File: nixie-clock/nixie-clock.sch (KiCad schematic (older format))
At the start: 69 parts, among them J1 Barrel_Jack, J2 Conn_01x02, J3 Conn_01x02, Q1 2N7002, Q2 2N7002, Q3 2N7002, Q4 2N7002, Q5 2N7002, Q6 Q_Photo_NPN, Q7 PSMN014-80YL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

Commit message: Top layer ground plane and stitching
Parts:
- added J4, J5, J6, J7, J8: Conn_01x01_MountingPin, custom-parts:4MM_Mounting_Hole, symbol Connector_Generic_MountingPin:Conn_01x01_MountingPin
- U1: symbol RF_Module:ESP32-WROOM-32D -> custom-parts:ESP32-WROOM-32D
- U6: footprint Package_SO:SOIC-16W_7.5x10.3mm_P1.27mm -> Package_SO:SO-8_5.3x6.2mm_P1.27mm; symbol Timer_RTC:DS3231M -> Timer_RTC:DS3231MZ
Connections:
- net RTL_RST is gone; now on net RTC_RST: U6.4 (~RST)
- net +3V3: now also U6.6 (VBAT); no longer U6.2 (VCC)
- net GND: now also U1.39 (GND), U6.2 (VCC), J4.1 (Pin_1), J4.MP (MountPin), J5.1 (Pin_1), J5.MP (MountPin), J6.1 (Pin_1), J6.MP (MountPin), J7.1 (Pin_1), J7.MP (MountPin), J8.1 (Pin_1), J8.MP (MountPin); no longer U6.10 (GND), U6.11 (GND), U6.12 (GND), U6.13 (GND), U6.14 (VBAT), U6.6 (GND), U6.7 (GND), U6.8 (GND), U6.9 (GND)
- net RTC_INT: now also U1.9 (IO33); no longer U1.37 (IO23)
- net RTC_SCL: now also U6.8 (SCL); no longer U6.16 (SCL)
- net RTC_SDA: now also R8.2, U6.7 (SDA)
- net at U2.28 (CLK), U3.28 (CLK): now also Q2.3 (D), R2.2; no longer Q1.3 (D), R1.2
- removed net RTL_SDA: R8.2, U6.15 (SDA)
- new net: Q1.3 (D), R1.2, U2.32 (DATA_IN)
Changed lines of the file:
@@
 $EndDescr
 $Comp
-L RF_Module:ESP32-WROOM-32D U1
+L custom-parts:ESP32-WROOM-32D U1
 U 1 1 5C1B096D
 P 1750 2500
@@
 Wire Wire Line
 	4700 3400 7850 3400
-Wire Wire Line
-	7850 3400 7850 1550
-Wire Wire Line
-	7850 1550 8850 1550
 Connection ~ 4300 1750
 Wire Wire Line
 	4300 1750 4300 1800
 Wire Wire Line
-	7750 1450 7750 3300
-Wire Wire Line
 	7750 3300 3950 3300
 Wire Wire Line
@@
 	3950 1750 3500 1750
 Wire Wire Line
-	7750 1450 8700 1450
+	7850 1450 8700 1450
 Connection ~ 3500 1750
 Wire Wire Line
@@
 $EndComp
 $Comp
-L Timer_RTC:DS3231M U6
+L Timer_RTC:DS3231MZ U6
 U 1 1 5C31CD5B
 P 2500 8100
 F 0 "U6" H 2500 7614 50  0000 C CNN
 F 1 "DS3231M" H 2500 7523 50  0000 C CNN
-F 2 "Package_SO:SOIC-16W_7.5x10.3mm_P1.27mm" H 2500 7500 50  0001 C CNN
+F 2 "Package_SO:SO-8_5.3x6.2mm_P1.27mm" H 2500 7500 50  0001 C CNN
 F 3 "http://datasheets.maximintegrated.com/en/ds/DS3231.pdf" H 2770 8150 50  0001 C CNN
 	1    2500 8100
@@
 RTC_SCL
 Text Label 1200 8000 0    50   ~ 0
-RTL_SDA
+RTC_SDA
 Text Label 1200 8300 0    50   ~ 0
-RTL_RST
+RTC_RST
 Wire Wire Line
 	2850 5850 3100 5850
@@
 	2350 3000 2450 3000
 Wire Wire Line
-	2350 2900 2450 2900
-Text Label 2450 2900 0    50   ~ 0
+	2350 3400 2450 3400
+Text Label 2450 3400 0    50   ~ 0
 RTC_INT
 Text Label 2450 3000 0    50   ~ 0
@@
 Wire Wire Line
 	9450 1000 9450 1050
+Wire Wire Line
+	7750 3300 7750 1550
+Wire Wire Line
+	7750 1550 8850 1550
+Wire Wire Line
+	7850 3400 7850 1450
+$Comp
+L Connector_Generic_MountingPin:Conn_01x01_MountingPin J4
+U 1 1 5C4AB747
+P 11500 12650
+F 0 "J4" H 11587 12616 50  0000 L CNN
+F 1 "Conn_01x01_MountingPin" H 11587 12525 50  0000 L CNN
+F 2 "custom-parts:4MM_Mounting_Hole" H 11500 12650 50  0001 C CNN
+F 3 "~" H 11500 12650 50  0001 C CNN
+	1    11500 12650
+	1    0    0    -1
+$EndComp
+$Comp
+L Connector_Generic_MountingPin:Conn_01x01_MountingPin J5
+U 1 1 5C4AB84B
+P 12800 12650
+F 0 "J5" H 12887 12616 50  0000 L CNN
+F 1 "Conn_01x01_MountingPin" H 12887 12525 50  0000 L CNN
+F 2 "custom-parts:4MM_Mounting_Hole" H 12800 12650 50  0001 C CNN
+F 3 "~" H 12800 12650 50  0001 C CNN
+	1    12800 12650
+	1    0    0    -1
+$EndComp
+$Comp
+L Connector_Generic_MountingPin:Conn_01x01_MountingPin J6
+U 1 1 5C4AB90F
+P 14100 12650
+F 0 "J6" H 14187 12616 50  0000 L CNN
+F 1 "Conn_01x01_MountingPin" H 14187 12525 50  0000 L CNN
+F 2 "custom-parts:4MM_Mounting_Hole" H 14100 12650 50  0001 C CNN
+F 3 "~" H 14100 12650 50  0001 C CNN
+	1    14100 12650
+	1    0    0    -1
+$EndComp
+$Comp
+L Connector_Generic_MountingPin:Conn_01x01_MountingPin J7
+U 1 1 5C4AB9DB
+P 15400 12650
+F 0 "J7" H 15487 12616 50  0000 L CNN
+F 1 "Conn_01x01_MountingPin" H 15487 12525 50  0000 L CNN
+F 2 "custom-parts:4MM_Mounting_Hole" H 15400 12650 50  0001 C CNN
+F 3 "~" H 15400 12650 50  0001 C CNN
+	1    15400 12650
+	1    0    0    -1
+$EndComp
+$Comp
+L power:GND #PWR0144
+U 1 1 5C4AC4F4
+P 11500 12950
+F 0 "#PWR0144" H 11500 12700 50  0001 C CNN
+F 1 "GND" H 11505 12777 50  0000 C CNN
+F 2 "" H 11500 12950 50  0001 C CNN
+F 3 "" H 11500 12950 50  0001 C CNN
+	1    11500 12950
+	1    0    0    -1
+$EndComp
+$Comp
+L power:GND #PWR0145
+U 1 1 5C4AC598
+P 12800 12950
+F 0 "#PWR0145" H 12800 12700 50  0001 C CNN
+F 1 "GND" H 12805 12777 50  0000 C CNN
+F 2 "" H 12800 12950 50  0001 C CNN
+F 3 "" H 12800 12950 50  0001 C CNN
+	1    12800 12950
+	1    0    0    -1
+$EndComp
+$Comp
+L power:GND #PWR0146
+U 1 1 5C4AC635
+P 14100 12950
+F 0 "#PWR0146" H 14100 12700 50  0001 C CNN
+F 1 "GND" H 14105 12777 50  0000 C CNN
+F 2 "" H 14100 12950 50  0001 C CNN
+F 3 "" H 14100 12950 50  0001 C CNN
+	1    14100 12950
+	1    0    0    -1
+$EndComp
+$Comp
+L power:GND #PWR0147
+U 1 1 5C4AC6D2
+P 15400 12950
+F 0 "#PWR0147" H 15400 12700 50  0001 C CNN
+F 1 "GND" H 15405 12777 50  0000 C CNN
+F 2 "" H 15400 12950 50  0001 C CNN
+F 3 "" H 15400 12950 50  0001 C CNN
+	1    15400 12950
+	1    0    0    -1
+$EndComp
+Wire Wire Line
+	11300 12650 11300 12850
+Wire Wire Line
+	11300 12850 11500 12850
+Wire Wire Line
+	11500 12950 11500 12850
+Connection ~ 11500 12850
+Wire Wire Line
+	12600 12650 12600 12850
+Wire Wire Line
+	12600 12850 12800 12850
+Wire Wire Line
+	12800 12850 12800 12950
+Connection ~ 12800 12850
+Wire Wire Line
+	13900 12650 13900 12850
+Wire Wire Line
+	13900 12850 14100 12850
+Wire Wire Line
+	14100 12950 14100 12850
+Connection ~ 14100 12850
+Wire Wire Line
+	15200 12650 15200 12850
+Wire Wire Line
+	15200 12850 15400 12850
+Wire Wire Line
+	15400 12850 15400 12950
+Connection ~ 15400 12850
+$Comp
+L Connector_Generic_MountingPin:Conn_01x01_MountingPin J8
+U 1 1 5C4B3E54
+P 16700 12650
+F 0 "J8" H 16787 12616 50  0000 L CNN
+F 1 "Conn_01x01_MountingPin" H 16787 12525 50  0000 L CNN
+F 2 "custom-parts:4MM_Mounting_Hole" H 16700 12650 50  0001 C CNN
+F 3 "~" H 16700 12650 50  0001 C CNN
+	1    16700 12650
+	1    0    0    -1
+$EndComp
+$Comp
+L power:GND #PWR0148
+U 1 1 5C4B3E5A
+P 16700 12950
+F 0 "#PWR0148" H 16700 12700 50  0001 C CNN
+F 1 "GND" H 16705 12777 50  0000 C CNN
+F 2 "" H 16700 12950 50  0001 C CNN
+F 3 "" H 16700 12950 50  0001 C CNN
+	1    16700 12950
+	1    0    0    -1
+$EndComp
+Wire Wire Line
+	16500 12650 16500 12850
+Wire Wire Line
+	16500 12850 16700 12850
+Wire Wire Line
+	16700 12850 16700 12950
+Connection ~ 16700 12850
 $EndSCHEMATC

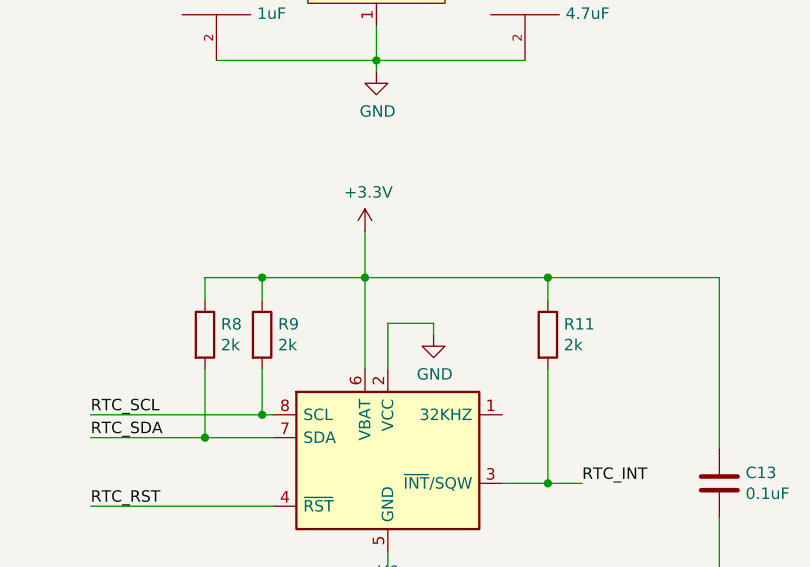
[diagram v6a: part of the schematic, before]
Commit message: Nixie Clock Fixes / Tweaks
- Connect TPS40210 power pad to ground.
- Exact board outlines
- Remove refs from mounting holes
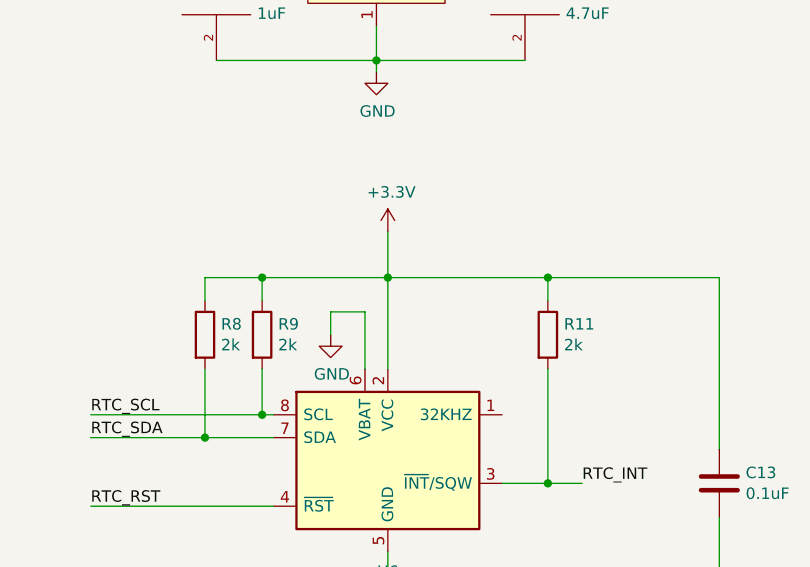
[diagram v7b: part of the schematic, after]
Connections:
- net +3V3: now also U6.2 (VCC); no longer U6.6 (VBAT)
- net GND: now also U6.6 (VBAT); no longer U6.2 (VCC)
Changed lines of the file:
@@
 L power:+3.3V #PWR0134
 U 1 1 5C729FDB
-P 2400 7100
-F 0 "#PWR0134" H 2400 6950 50  0001 C CNN
-F 1 "+3.3V" H 2415 7273 50  0000 C CNN
-F 2 "" H 2400 7100 50  0001 C CNN
-F 3 "" H 2400 7100 50  0001 C CNN
-	1    2400 7100
-	1    0    0    -1
-$EndComp
-Wire Wire Line
-	2400 7100 2400 7300
+P 2500 7100
+F 0 "#PWR0134" H 2500 6950 50  0001 C CNN
+F 1 "+3.3V" H 2515 7273 50  0000 C CNN
+F 2 "" H 2500 7100 50  0001 C CNN
+F 3 "" H 2500 7100 50  0001 C CNN
+	1    2500 7100
+	1    0    0    -1
+$EndComp
+Wire Wire Line
+	2500 7100 2500 7300
 $Comp
 L power:GND #PWR0135
@@
 Text Label 3350 8200 0    50   ~ 0
 RTC_INT
-$Comp
-L power:GND #PWR0136
-U 1 1 5C7BD655
-P 2700 7550
-F 0 "#PWR0136" H 2700 7300 50  0001 C CNN
-F 1 "GND" H 2705 7377 50  0000 C CNN
-F 2 "" H 2700 7550 50  0001 C CNN
-F 3 "" H 2700 7550 50  0001 C CNN
-	1    2700 7550
-	1    0    0    -1
-$EndComp
-Wire Wire Line
-	2700 7550 2700 7500
-Wire Wire Line
-	2700 7500 2500 7500
-Wire Wire Line
-	2500 7500 2500 7700
 Wire Wire Line
 	1200 7900 1950 7900
@@
 	1    0    0    -1
 $EndComp
-Connection ~ 2400 7300
-Wire Wire Line
-	2400 7300 2400 7700
+Connection ~ 2500 7300
 Wire Wire Line
 	1700 7400 1700 7300
@@
 Connection ~ 1950 7300
 Wire Wire Line
-	1950 7300 2400 7300
+	1950 7300 2500 7300
 Wire Wire Line
 	3200 7400 3200 7300
 Wire Wire Line
-	3200 7300 2400 7300
+	3200 7300 2500 7300
 Wire Wire Line
 	3200 7700 3200 8200
@@
 	16700 12850 16700 12950
 Connection ~ 16700 12850
+Wire Wire Line
+	2500 7300 2500 7700
+$Comp
+L power:GND #PWR0136
+U 1 1 5C5FD223
+P 2250 7550
+F 0 "#PWR0136" H 2250 7300 50  0001 C CNN
+F 1 "GND" H 2255 7377 50  0000 C CNN
+F 2 "" H 2250 7550 50  0001 C CNN
+F 3 "" H 2250 7550 50  0001 C CNN
+	1    2250 7550
+	1    0    0    -1
+$EndComp
+Wire Wire Line
+	2250 7550 2250 7450
+Wire Wire Line
+	2250 7450 2400 7450
+Wire Wire Line
+	2400 7450 2400 7700
 $EndSCHEMATC

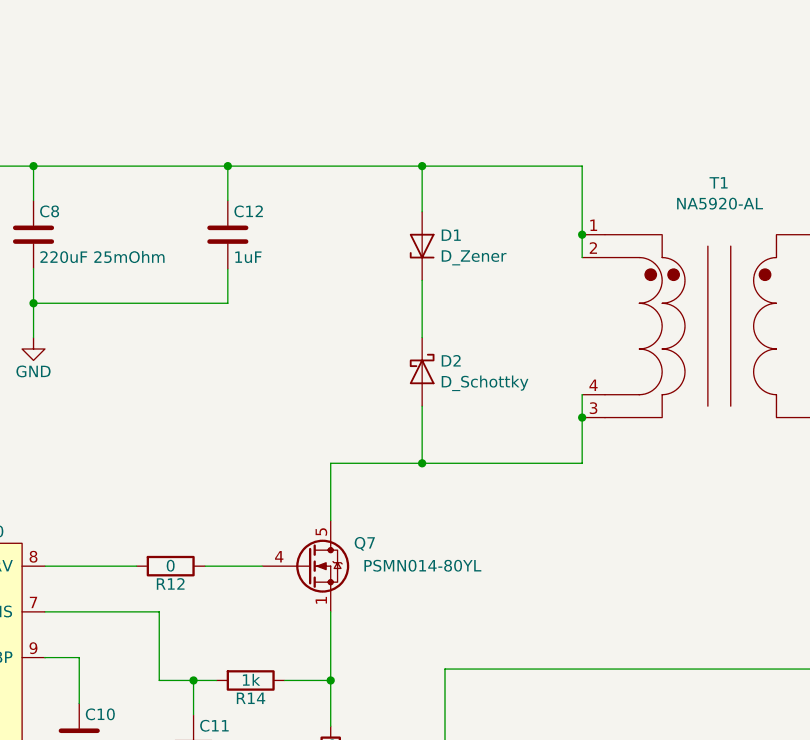
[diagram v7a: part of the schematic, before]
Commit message: HV power supply works, swap tubes to other side of board
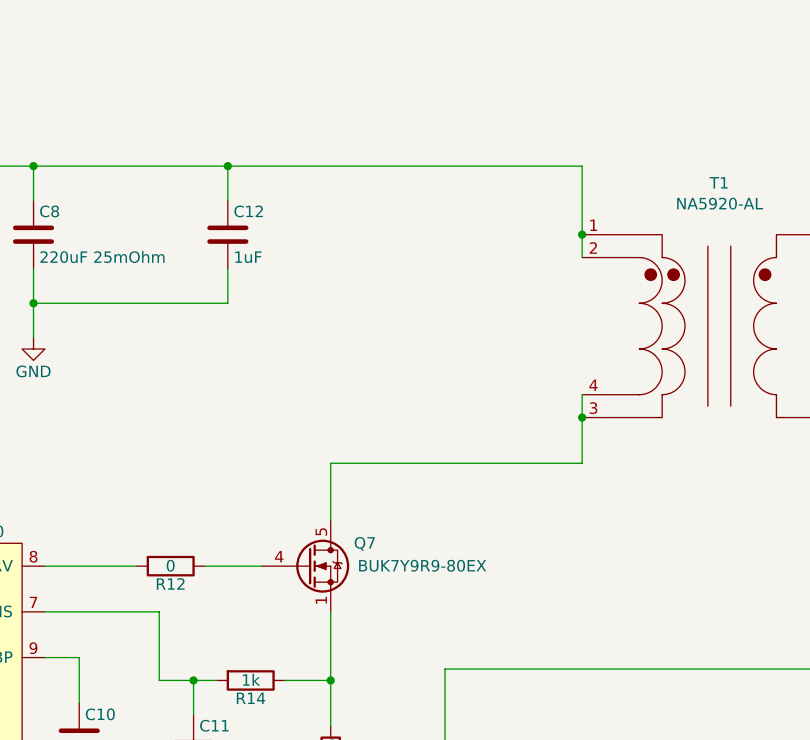
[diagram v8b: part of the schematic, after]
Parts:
- removed D1: D_Zener, Diode_SMD:D_SOD-123, symbol Device:D_Zener
- removed D2: D_Schottky, Diode_SMD:D_1206_3216Metric_Castellated, symbol Device:D_Schottky
- Q7: value PSMN014-80YL -> BUK7Y9R9-80EX
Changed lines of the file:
@@
 P 4100 13550
 F 0 "Q7" H 4350 13650 50  0000 C CNN
-F 1 "PSMN014-80YL" H 4600 13550 50  0000 C CNN
+F 1 "BUK7Y9R9-80EX" H 4600 13550 50  0000 C CNN
 F 2 "Package_TO_SOT_SMD:LFPAK56" H 4200 14000 50  0001 C CNN
 F 3 "https://assets.nexperia.com/documents/data-sheet/PSMN5R2-60YL.pdf" H 4100 13550 50  0001 C CNN
@@
 	1    0    0    -1
 $EndComp
-Wire Wire Line
-	5300 13100 4600 13100
 Wire Wire Line
 	4200 13100 4200 13350
@@
 Wire Wire Line
 	750  11650 750  11800
-Wire Wire Line
-	5300 11800 4600 11800
 Connection ~ 750  11800
 Wire Wire Line
@@
 	2550 4000 2550 4100
 $Comp
-L Device:D_Zener D1
-U 1 1 5C45A07C
-P 4600 12150
-F 0 "D1" V 4646 12071 50  0000 R CNN
-F 1 "D_Zener" V 4555 12071 50  0000 R CNN
-F 2 "Diode_SMD:D_SOD-123" H 4600 12150 50  0001 C CNN
-F 3 "~" H 4600 12150 50  0001 C CNN
-F 4 "BZT52-B75J" V 4600 12150 50  0001 C CNN "Part Number"
-	1    4600 12150
-	0    -1   -1   0
-$EndComp
-$Comp
-L Device:D_Schottky D2
-U 1 1 5C45A278
-P 4600 12700
-F 0 "D2" V 4554 12779 50  0000 L CNN
-F 1 "D_Schottky" V 4645 12779 50  0000 L CNN
-F 2 "Diode_SMD:D_1206_3216Metric_Castellated" H 4600 12700 50  0001 C CNN
-F 3 "~" H 4600 12700 50  0001 C CNN
-F 4 "CD1206-B2100" V 4600 12700 50  0001 C CNN "Part Number"
-	1    4600 12700
-	0    1    1    0
-$EndComp
-Wire Wire Line
-	4600 11800 4600 12000
-Connection ~ 4600 11800
-Wire Wire Line
-	4600 11800 3750 11800
-Wire Wire Line
-	4600 12300 4600 12550
-Wire Wire Line
-	4600 12850 4600 13100
-Connection ~ 4600 13100
-Wire Wire Line
-	4600 13100 4200 13100
-$Comp
 L Device:C C19
 U 1 1 5C4A5A14
@@
 Wire Wire Line
 	2400 7450 2400 7700
+Wire Wire Line
+	3750 11800 5300 11800
+Wire Wire Line
+	4200 13100 5300 13100
 $EndSCHEMATC
